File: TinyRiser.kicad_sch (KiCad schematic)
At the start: 22 parts, among them J2 Bus_PCI_Express_x16, J3 Bus_M.2_Socket_M

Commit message: Adding fan header (unfinished)
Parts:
- added J4: fancontrol_header, Connector_PinSocket_2.54mm:PinSocket_2x03_P2.54mm_Horizontal, symbol Connector_Generic:Conn_02x03_Odd_Even
- added M1: Fan_4pin, Connector:FanPinHeader_1x04_P2.54mm_Vertical, symbol Motor:Fan_4pin
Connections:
- net +12V: now also J4.2 (Pin_2)
- net GND: now also M1.1 (-)
- new net +12V_fan: J4.1 (Pin_1), M1.2 (+)

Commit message: Mostly finished fan connector implementation
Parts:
- added R6: 0R, Resistor_SMD:R_0603_1608Metric_Pad0.98x0.95mm_HandSolder, symbol Device:R
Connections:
- net +12V_fan: now also J4.5 (Pin_5); no longer J4.1 (Pin_1)
- net +3V3: now also J4.4 (Pin_4)
- net GND: now also J4.6 (Pin_6)
- net Taco_fan: now reaches J4.3 (Pin_3)
- net Taco_fan: now also M1.3 (Tacho)
- net PWM_fan: now reaches M1.4 (PWM)
- net PWM_fan: now also J4.1 (Pin_1)

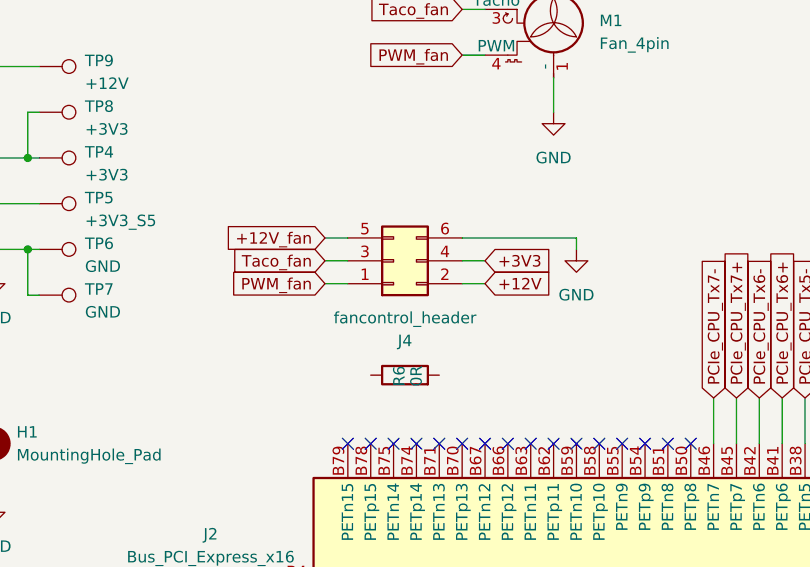
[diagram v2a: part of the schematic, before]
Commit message: swapped fan header for right angle pin header
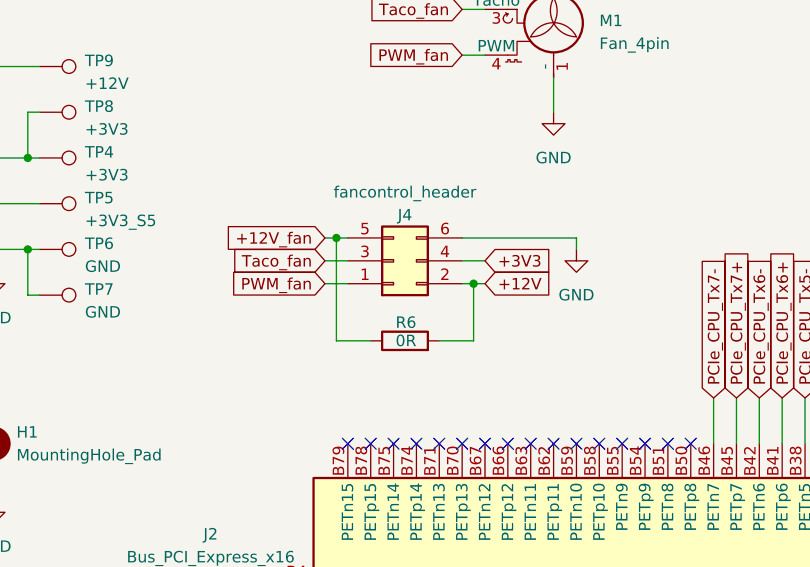
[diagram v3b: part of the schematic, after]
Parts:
- M1: footprint Connector:FanPinHeader_1x04_P2.54mm_Vertical -> Connector_PinHeader_2.54mm:PinHeader_1x04_P2.54mm_Horizontal
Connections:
- net +12V: now also R6.2
- net +12V_fan: now also R6.1
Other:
- moved on the sheet: R6
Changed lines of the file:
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@@
 	)
 	(junction
+		(at 203.2 52.07)
+		(diameter 0)
+		(color 0 0 0 0)
+	)
+	(junction
 		(at 130.81 224.79)
 		(diameter 0)
@@
 	)
 	(junction
+		(at 218.44 57.15)
+		(diameter 0)
+		(color 0 0 0 0)
+	)
+	(junction
 		(at 293.37 71.12)
 		(diameter 0)
@@
 	(wire
 		(pts
-			(xy 204.47 57.15) (xy 201.93 57.15)
-		)
-		(stroke
-			(width 0)
-			(type default)
-		)
-	)
-	(wire
-		(pts
 			(xy 137.16 172.72) (xy 137.16 177.8)
 		)
@@
 	(wire
 		(pts
+			(xy 218.44 63.5) (xy 218.44 57.15)
+		)
+		(stroke
+			(width 0)
+			(type default)
+		)
+	)
+	(wire
+		(pts
 			(xy 270.51 105.41) (xy 270.51 110.49)
 		)
@@
 	(wire
 		(pts
+			(xy 207.01 63.5) (xy 203.2 63.5)
+		)
+		(stroke
+			(width 0)
+			(type default)
+		)
+	)
+	(wire
+		(pts
 			(xy 276.86 172.72) (xy 276.86 177.8)
 		)
@@
 	(wire
 		(pts
+			(xy 203.2 52.07) (xy 204.47 52.07)
+		)
+		(stroke
+			(width 0)
+			(type default)
+		)
+	)
+	(wire
+		(pts
 			(xy 247.65 69.85) (xy 247.65 74.93)
 		)
@@
 	(wire
 		(pts
+			(xy 218.44 57.15) (xy 217.17 57.15)
+		)
+		(stroke
+			(width 0)
+			(type default)
+		)
+	)
+	(wire
+		(pts
 			(xy 180.34 176.53) (xy 187.96 176.53)
 		)
@@
 	(wire
 		(pts
+			(xy 214.63 63.5) (xy 218.44 63.5)
+		)
+		(stroke
+			(width 0)
+			(type default)
+		)
+	)
+	(wire
+		(pts
 			(xy 82.55 36.83) (xy 82.55 44.45)
 		)
@@
 	(wire
 		(pts
-			(xy 219.71 57.15) (xy 217.17 57.15)
+			(xy 219.71 57.15) (xy 218.44 57.15)
 		)
 		(stroke
@@
 	(wire
 		(pts
-			(xy 201.93 52.07) (xy 204.47 52.07)
+			(xy 201.93 52.07) (xy 203.2 52.07)
 		)
 		(stroke
@@
 	(wire
 		(pts
+			(xy 201.93 57.15) (xy 204.47 57.15)
+		)
+		(stroke
+			(width 0)
+			(type default)
+		)
+	)
+	(wire
+		(pts
 			(xy 281.94 176.53) (xy 274.32 176.53)
 		)
@@
 	(wire
 		(pts
+			(xy 203.2 63.5) (xy 203.2 52.07)
+		)
+		(stroke
+			(width 0)
+			(type default)
+		)
+	)
+	(wire
+		(pts
 			(xy 170.18 172.72) (xy 170.18 177.8)
 		)
@@
 		(dnp no)
 		(property "Reference" "J4"
-			(at 210.82 63.5 0)
+			(at 210.82 49.53 0)
 			(effects
 				(font
@@
 		)
 		(property "Value" "fancontrol_header"
-			(at 210.82 60.96 0)
+			(at 210.82 46.99 0)
 			(effects
 				(font
@@
 	(symbol
 		(lib_id "Device:R")
-		(at 210.82 67.31 90)
+		(at 210.82 63.5 90)
 		(unit 1)
 		(exclude_from_sim no)
@@
 		(dnp no)
 		(property "Reference" "R6"
-			(at 210.185 68.58 0)
+			(at 212.09 61.468 90)
 			(effects
 				(font
@@
 		)
 		(property "Value" "0R"
-			(at 212.09 68.58 0)
+			(at 212.09 63.5 90)
 			(effects
 				(font
@@
 		)
 		(property "Footprint" "Resistor_SMD:R_0603_1608Metric_Pad0.98x0.95mm_HandSolder"
-			(at 210.82 69.088 90)
+			(at 210.82 65.278 90)
 			(effects
 				(font
@@
 		)
 		(property "Datasheet" "~"
-			(at 210.82 67.31 0)
+			(at 210.82 63.5 0)
 			(effects
 				(font
@@
 		)
 		(property "Description" ""
-			(at 210.82 67.31 0)
+			(at 210.82 63.5 0)
 			(effects
 				(font
@@
 			)
 		)
-		(property "Footprint" "Connector:FanPinHeader_1x04_P2.54mm_Vertical"
+		(property "Footprint" "Connector_PinHeader_2.54mm:PinHeader_1x04_P2.54mm_Horizontal"
 			(at 227.33 28.956 0)
 			(effects

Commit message: Finished fan header implementation
Somehow it doesn't feel like it's done but it is???
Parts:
- R2: renamed from R6; footprint Resistor_SMD:R_0603_1608Metric_Pad0.98x0.95mm_HandSolder -> Resistor_SMD:R_0805_2012Metric_Pad1.20x1.40mm_HandSolder
- renumbered R2 to R3, R3 to R4, R4 to R5, R5 to R6
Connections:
- net +12V_fan: now also J4.1 (Pin_1); no longer J4.5 (Pin_5)
- net PWM_fan: now also J4.5 (Pin_5); no longer J4.1 (Pin_1)
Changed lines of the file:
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@@
 	)
 	(junction
-		(at 203.2 52.07)
-		(diameter 0)
-		(color 0 0 0 0)
-	)
-	(junction
 		(at 130.81 224.79)
 		(diameter 0)
@@
 	)
 	(junction
+		(at 203.2 57.15)
+		(diameter 0)
+		(color 0 0 0 0)
+	)
+	(junction
 		(at 238.76 176.53)
 		(diameter 0)
@@
 	(wire
 		(pts
+			(xy 203.2 57.15) (xy 204.47 57.15)
+		)
+		(stroke
+			(width 0)
+			(type default)
+		)
+	)
+	(wire
+		(pts
 			(xy 213.36 223.52) (xy 213.36 228.6)
 		)
@@
 	(wire
 		(pts
-			(xy 203.2 52.07) (xy 204.47 52.07)
+			(xy 201.93 52.07) (xy 204.47 52.07)
 		)
 		(stroke
@@
 	(wire
 		(pts
-			(xy 201.93 52.07) (xy 203.2 52.07)
-		)
-		(stroke
-			(width 0)
-			(type default)
-		)
-	)
-	(wire
-		(pts
 			(xy 246.38 176.53) (xy 251.46 176.53)
 		)
@@
 	(wire
 		(pts
+			(xy 203.2 63.5) (xy 203.2 57.15)
+		)
+		(stroke
+			(width 0)
+			(type default)
+		)
+	)
+	(wire
+		(pts
 			(xy 107.95 102.87) (xy 113.03 102.87)
 		)
@@
 	(wire
 		(pts
-			(xy 201.93 57.15) (xy 204.47 57.15)
+			(xy 201.93 57.15) (xy 203.2 57.15)
 		)
 		(stroke
@@
 	(wire
 		(pts
-			(xy 203.2 63.5) (xy 203.2 52.07)
-		)
-		(stroke
-			(width 0)
-			(type default)
-		)
-	)
-	(wire
-		(pts
 			(xy 170.18 172.72) (xy 170.18 177.8)
 		)
@@
 	(global_label "+12V_fan"
 		(shape input)
-		(at 201.93 52.07 180)
+		(at 201.93 57.15 180)
 		(fields_autoplaced yes)
 		(effects
@@
 		)
 		(property "Intersheetrefs" "${INTERSHEET_REFS}"
-			(at 189.8735 52.07 0)
+			(at 189.8735 57.15 0)
 			(effects
 				(font
@@
 	(global_label "PWM_fan"
 		(shape input)
-		(at 201.93 57.15 180)
+		(at 201.93 52.07 180)
 		(fields_autoplaced yes)
 		(effects
@@
 		)
 		(property "Intersheetrefs" "${INTERSHEET_REFS}"
-			(at 190.7807 57.15 0)
+			(at 190.7807 52.07 0)
 			(effects
 				(font
@@
 		(on_board yes)
 		(dnp no)
-		(property "Reference" "R4"
+		(property "Reference" "R5"
 			(at 292.1 65.405 0)
 			(effects
@@
 			(project "TinyRiser"
 				(path "/881240ea-c4b5-4af2-848a-893b6d69814c"
-					(reference "R4")
+					(reference "R5")
 					(unit 1)
 				)
@@
 		(on_board yes)
 		(dnp no)
-		(property "Reference" "R2"
+		(property "Reference" "R3"
 			(at 287.02 65.405 0)
 			(effects
@@
 			(project "TinyRiser"
 				(path "/881240ea-c4b5-4af2-848a-893b6d69814c"
-					(reference "R2")
+					(reference "R3")
 					(unit 1)
 				)
@@
 		(on_board yes)
 		(dnp no)
-		(property "Reference" "R6"
+		(property "Reference" "R2"
 			(at 212.09 61.468 90)
 			(effects
@@
 			)
 		)
-		(property "Footprint" "Resistor_SMD:R_0603_1608Metric_Pad0.98x0.95mm_HandSolder"
+		(property "Footprint" "Resistor_SMD:R_0805_2012Metric_Pad1.20x1.40mm_HandSolder"
 			(at 210.82 65.278 90)
 			(effects
@@
 			(project "TinyRiser"
 				(path "/881240ea-c4b5-4af2-848a-893b6d69814c"
-					(reference "R6")
+					(reference "R2")
 					(unit 1)
 				)
@@
 		(on_board yes)
 		(dnp no)
-		(property "Reference" "R3"
+		(property "Reference" "R4"
 			(at 289.56 65.405 0)
 			(effects
@@
 			(project "TinyRiser"
 				(path "/881240ea-c4b5-4af2-848a-893b6d69814c"
-					(reference "R3")
+					(reference "R4")
 					(unit 1)
 				)
@@
 		(on_board yes)
 		(dnp no)
-		(property "Reference" "R5"
+		(property "Reference" "R6"
 			(at 294.64 65.405 0)
 			(effects
@@
 			(project "TinyRiser"
 				(path "/881240ea-c4b5-4af2-848a-893b6d69814c"
-					(reference "R5")
+					(reference "R6")
 					(unit 1)
 				)
